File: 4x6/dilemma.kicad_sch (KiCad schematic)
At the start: 310 parts, among them J1 USB_C_Receptacle_USB2.0, J102 NA_serial, J105 NA_Conn_01x04_Female, J113 Cirque, J2 NA_Conn_01x03_Female, J3 NA_GC9A01, J4 Conn_01x05, J5 NA_Conn_01x02, J5001 USB_C_Receptacle_USB2.0, J5002 NA_Conn_01x02, J5003 NA_serial, J5004 NA_GC9A01, J5005 NA_Conn_01x04_Female, J5006 NA_Conn_01x03_Female, J5007 Cirque, J5008 Conn_01x05, J5009 Conn_01x05, J5010 Conn_01x05, SW1 SW_Push, SW101 NA_SW_Push, SW102 NA_SW_Push, SW103 NA_SW_Push, SW104 NA_SW_Push, SW105 NA_SW_Push, SW106 NA_SW_Push, SW107 NA_SW_Push, SW108 NA_SW_Push, SW109 NA_SW_Push, SW112 NA_SW_Push, SW113 NA_SW_Push, SW114 NA_SW_Push, SW115 NA_SW_Push, SW116 NA_SW_Push, SW117 NA_SW_Push, SW118 NA_SW_Push, SW119 NA_SW_Push, SW3001 NA_SW_Push, SW3002 NA_RotaryEncoder_Switch, SW5001 SW_Push, SW5002 NA_SW_Push, SW5003 NA_SW_Push, SW5004 NA_SW_Push, SW5005 NA_SW_Push, SW5006 NA_SW_Push, SW5007 NA_SW_Push, SW5008 NA_SW_Push, SW5009 NA_SW_Push, SW5010 NA_SW_Push, SW5011 NA_SW_Push, SW5012 NA_SW_Push, SW5013 NA_SW_Push, SW5014 NA_SW_Push, SW5015 NA_SW_Push, SW5016 NA_SW_Push, SW5017 NA_SW_Push, SW5018 NA_SW_Push, SW5019 NA_SW_Push, SW5020 NA_RotaryEncoder_Switch, SW5021 SW_SPST, SW5022 SW_SPST, SW5023 NA_SW_Push, SW5024 NA_SW_Push, SW5025 NA_SW_Push, SW5026 NA_SW_Push, SW5027 NA_SW_Push, SW5028 NA_SW_Push, SW5029 NA_SW_Push, SW5030 NA_SW_Push, SW5031 NA_SW_Push, SW5032 NA_SW_Push, SW5033 NA_SW_Push, SW5034 NA_SW_Push, SW5035 NA_SW_Push, SW5036 NA_SW_Push, SW5037 NA_SW_Push, SW5038 NA_SW_Push, SW5039 NA_SW_Push, SW5040 NA_SW_Push, U1 RP2040, U2 W25Q128JVS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

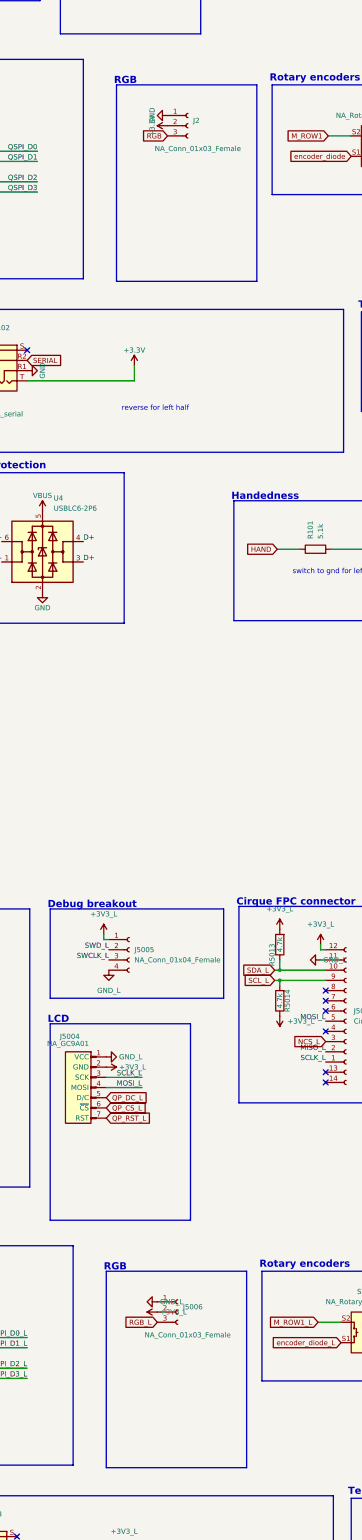
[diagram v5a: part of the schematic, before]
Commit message: underglow leds
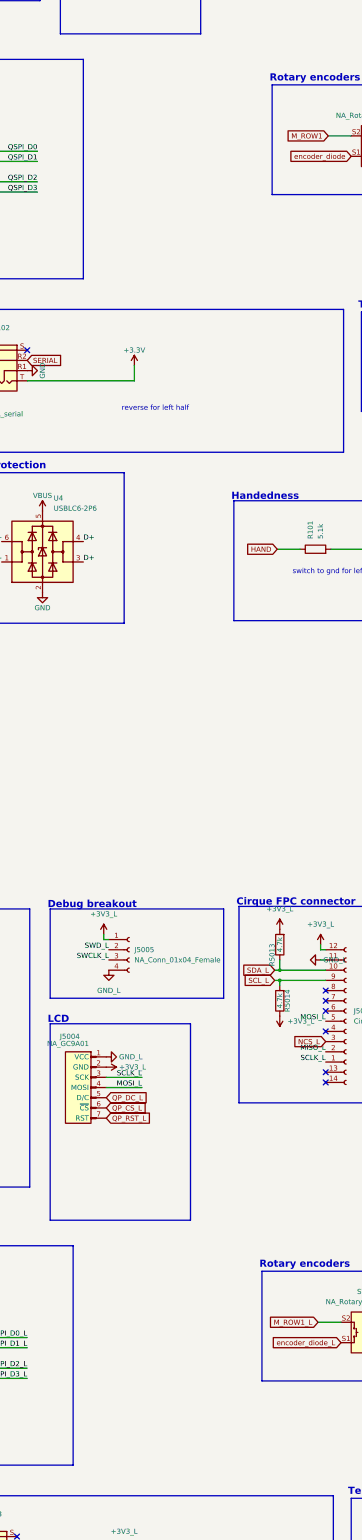
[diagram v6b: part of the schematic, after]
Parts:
- removed J2, J5006: NA_Conn_01x03_Female, local-libraries:PinHeader_1x03_P2.54mm_Vertical_smd, symbol Connector:Conn_01x03_Female
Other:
- note removed: "RGB"
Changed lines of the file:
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@@
     (stroke (width 0) (type default))
   )
-  (polyline (pts (xy 322.58 159.385) (xy 287.655 159.385))
-    (stroke (width 0) (type default))
-  )
   (wire (pts (xy 819.785 36.195) (xy 822.325 36.195))
     (stroke (width 0) (type default))
@@
     (stroke (width 0) (type default))
   )
-  (polyline (pts (xy 322.58 110.49) (xy 322.58 159.385))
-    (stroke (width 0) (type default))
-  )
   (wire (pts (xy 190.5 220.98) (xy 195.58 220.98))
     (stroke (width 0) (type default))
@@
     (stroke (width 0) (type default))
   )
-  (polyline (pts (xy 320.04 405.765) (xy 320.04 454.66))
-    (stroke (width 0) (type default))
-  )
   (wire (pts (xy 105.41 90.17) (xy 93.98 90.17))
     (stroke (width 0) (type default))
@@
     (stroke (width 0) (type default))
   )
-  (polyline (pts (xy 287.655 110.49) (xy 322.58 110.49))
-    (stroke (width 0) (type default))
-  )
   (wire (pts (xy 46.99 259.08) (xy 46.99 261.62))
     (stroke (width 0) (type default))
@@
     (stroke (width 0) (type default))
   )
-  (polyline (pts (xy 320.04 454.66) (xy 285.115 454.66))
-    (stroke (width 0) (type default))
-  )
   (wire (pts (xy 160.02 333.375) (xy 162.56 333.375))
     (stroke (width 0) (type default))
@@
     (stroke (width 0) (type default))
   )
-  (polyline (pts (xy 285.115 405.765) (xy 285.115 454.66))
-    (stroke (width 0) (type default))
-  )
   (wire (pts (xy 142.24 231.14) (xy 142.24 232.41))
     (stroke (width 0) (type default))
@@
     (stroke (width 0) (type default))
   )
-  (polyline (pts (xy 287.655 110.49) (xy 287.655 159.385))
-    (stroke (width 0) (type default))
-  )
   (wire (pts (xy 342.265 30.48) (xy 340.995 30.48))
     (stroke (width 0) (type default))
@@
     (stroke (width 0) (type default))
   )
-  (polyline (pts (xy 285.115 405.765) (xy 320.04 405.765))
-    (stroke (width 0) (type default))
-  )
   (polyline (pts (xy 15.24 315.595) (xy 78.74 315.595))
     (stroke (width 0) (type default))
@@
     (effects (font (size 1.778 1.778) (thickness 0.3556) bold) (justify left bottom))
   )
-  (text "RGB" (at 284.48 405.765 0)
-    (effects (font (size 1.778 1.778) (thickness 0.3556) bold) (justify left bottom))
-  )
   (text "switch to gnd for left half" (at 328.93 528.955 0)
     (effects (font (size 1.27 1.27)) (justify left bottom))
@@
     (effects (font (size 1.778 1.778) (thickness 0.3556) bold) (justify left bottom))
   )
-  (text "RGB" (at 287.02 110.49 0)
-    (effects (font (size 1.778 1.778) (thickness 0.3556) bold) (justify left bottom))
-  )
   (text "Rotary encoders" (at 323.215 405.13 0)
     (effects (font (size 1.778 1.778) (thickness 0.3556) bold) (justify left bottom))
@@
     )
   )
-  (global_label "RGB" (shape input) (at 300.355 123.19 180)
-    (effects (font (size 1.27 1.27)) (justify right))
-    (property "Intersheetrefs" "${INTERSHEET_REFS}" (at 212.725 55.88 0)
-      (effects (font (size 1.27 1.27)) hide)
-    )
-  )
   (global_label "SDA_L" (shape input) (at 327.025 330.835 180)
     (effects (font (size 1.27 1.27)) (justify right))
@@
     )
   )
-  (global_label "RGB_L" (shape input) (at 297.815 418.465 180)
-    (effects (font (size 1.27 1.27)) (justify right))
-    (property "Intersheetrefs" "${INTERSHEET_REFS}" (at 210.185 351.155 0)
-      (effects (font (size 1.27 1.27)) hide)
-    )
-  )
   (global_label "RGB_L" (shape input) (at 426.085 370.84 0)
     (effects (font (size 1.27 1.27)) (justify left))
@@
     )
   )
-  (symbol (lib_id "power_L:GND_L") (at 297.815 413.385 270) (unit 1)
-    (in_bom yes) (on_board yes) (dnp no) (fields_autoplaced)
-    (property "Reference" "#PWR05048" (at 291.465 413.385 0)
-      (effects (font (size 1.27 1.27)) hide)
-    )
-    (property "Value" "GND_L" (at 298.45 413.3849 90)
-      (effects (font (size 1.27 1.27)) (justify left))
-    )
-    (property "Footprint" "" (at 297.815 413.385 0)
-      (effects (font (size 1.27 1.27)) hide)
-    )
-    (property "Datasheet" "" (at 297.815 413.385 0)
-      (effects (font (size 1.27 1.27)) hide)
-    )
-    (pin "1")
-    (instances
-      (project "dilemma"
-        (path "/7353e96a-343a-4876-b497-b1d205a14d97"
-          (reference "#PWR05048") (unit 1)
-        )
-      )
-    )
-  )
   (symbol (lib_id "power:GND") (at 35.56 77.47 0) (unit 1)
     (in_bom yes) (on_board yes) (dnp no)
@@
     )
   )
-  (symbol (lib_id "power:GND") (at 300.355 118.11 270) (unit 1)
-    (in_bom yes) (on_board yes) (dnp no)
-    (property "Reference" "#PWR0129" (at 294.005 118.11 0)
-      (effects (font (size 1.27 1.27)) hide)
-    )
-    (property "Value" "GND" (at 296.545 118.11 0)
-      (effects (font (size 1.27 1.27)))
-    )
-    (property "Footprint" "" (at 300.355 118.11 0)
-      (effects (font (size 1.27 1.27)) hide)
-    )
-    (property "Datasheet" "" (at 300.355 118.11 0)
-      (effects (font (size 1.27 1.27)) hide)
-    )
-    (pin "1")
-    (instances
-      (project "dilemma"
-        (path "/7353e96a-343a-4876-b497-b1d205a14d97"
-          (reference "#PWR0129") (unit 1)
-        )
-      )
-    )
-  )
   (symbol (lib_id "power_L:GND_L") (at 181.61 474.345 0) (unit 1)
     (in_bom yes) (on_board yes) (dnp no) (fields_autoplaced)
@@
     )
   )
-  (symbol (lib_id "Connector:Conn_01x03_Female") (at 302.895 415.925 0) (unit 1)
-    (in_bom yes) (on_board yes) (dnp no)
-    (property "Reference" "J5006" (at 304.165 414.6549 0)
-      (effects (font (size 1.27 1.27)) (justify left))
-    )
-    (property "Value" "NA_Conn_01x03_Female" (at 294.64 421.64 0)
-      (effects (font (size 1.27 1.27)) (justify left))
-    )
-    (property "Footprint" "local-libraries:PinHeader_1x03_P2.54mm_Vertical_smd" (at 302.895 415.925 0)
-      (effects (font (size 1.27 1.27)) hide)
-    )
-    (property "Datasheet" "~" (at 302.895 415.925 0)
-      (effects (font (size 1.27 1.27)) hide)
-    )
-    (pin "1")
-    (pin "2")
-    (pin "3")
-    (instances
-      (project "dilemma"
-        (path "/7353e96a-343a-4876-b497-b1d205a14d97"
-          (reference "J5006") (unit 1)
-        )
-      )
-    )
-  )
   (symbol (lib_id "power:+1V1") (at 101.6 173.99 0) (unit 1)
     (in_bom yes) (on_board yes) (dnp no)
@@
     )
   )
-  (symbol (lib_id "power:+3.3V") (at 300.355 120.65 90) (unit 1)
-    (in_bom yes) (on_board yes) (dnp no)
-    (property "Reference" "#PWR0132" (at 304.165 120.65 0)
-      (effects (font (size 1.27 1.27)) hide)
-    )
-    (property "Value" "+3.3V" (at 296.545 120.65 0)
-      (effects (font (size 1.27 1.27)))
-    )
-    (property "Footprint" "" (at 300.355 120.65 0)
-      (effects (font (size 1.27 1.27)) hide)
-    )
-    (property "Datasheet" "" (at 300.355 120.65 0)
-      (effects (font (size 1.27 1.27)) hide)
-    )
-    (pin "1")
-    (instances
-      (project "dilemma"
-        (path "/7353e96a-343a-4876-b497-b1d205a14d97"
-          (reference "#PWR0132") (unit 1)
-        )
-      )
-    )
-  )
   (symbol (lib_id "power:+5V") (at 33.02 109.22 0) (unit 1)
     (in_bom yes) (on_board yes) (dnp no)
@@
     )
   )
-  (symbol (lib_id "Connector:Conn_01x03_Female") (at 305.435 120.65 0) (unit 1)
-    (in_bom yes) (on_board yes) (dnp no)
-    (property "Reference" "J2" (at 306.705 119.3799 0)
-      (effects (font (size 1.27 1.27)) (justify left))
-    )
-    (property "Value" "NA_Conn_01x03_Female" (at 297.18 126.365 0)
-      (effects (font (size 1.27 1.27)) (justify left))
-    )
-    (property "Footprint" "local-libraries:PinHeader_1x03_P2.54mm_Vertical_smd" (at 305.435 120.65 0)
-      (effects (font (size 1.27 1.27)) hide)
-    )
-    (property "Datasheet" "~" (at 305.435 120.65 0)
-      (effects (font (size 1.27 1.27)) hide)
-    )
-    (pin "1")
-    (pin "2")
-    (pin "3")
-    (instances
-      (project "dilemma"
-        (path "/7353e96a-343a-4876-b497-b1d205a14d97"
-          (reference "J2") (unit 1)
-        )
-      )
-    )
-  )
   (symbol (lib_id "power:GND") (at 254 31.115 270) (unit 1)
     (in_bom yes) (on_board yes) (dnp no)
@@
         )
       )
-    )
-  )
-  (symbol (lib_id "power_L:+3V3_L") (at 297.815 415.925 90) (unit 1)
-    (in_bom yes) (on_board yes) (dnp no) (fields_autoplaced)
-    (property "Reference" "#PWR05049" (at 301.625 415.925 0)
-      (effects (font (size 1.27 1.27)) hide)
-    )
-    (property "Value" "+3V3_L" (at 298.45 415.9249 90)
-      (effects (font (size 1.27 1.27)) (justify right))
-    )
-    (property "Footprint" "" (at 297.815 415.925 0)
-      (effects (font (size 1.27 1.27)) hide)
-    )
-    (property "Datasheet" "" (at 297.815 415.925 0)
-      (effects (font (size 1.27 1.27)) hide)
-    )
-    (pin "1")
-    (instances
-      (project "dilemma"
-        (path "/7353e96a-343a-4876-b497-b1d205a14d97"
-          (reference "#PWR05049") (unit 1)
-        )
-      )
